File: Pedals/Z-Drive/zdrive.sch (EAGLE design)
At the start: 27 parts, among them IC1 MC1458P

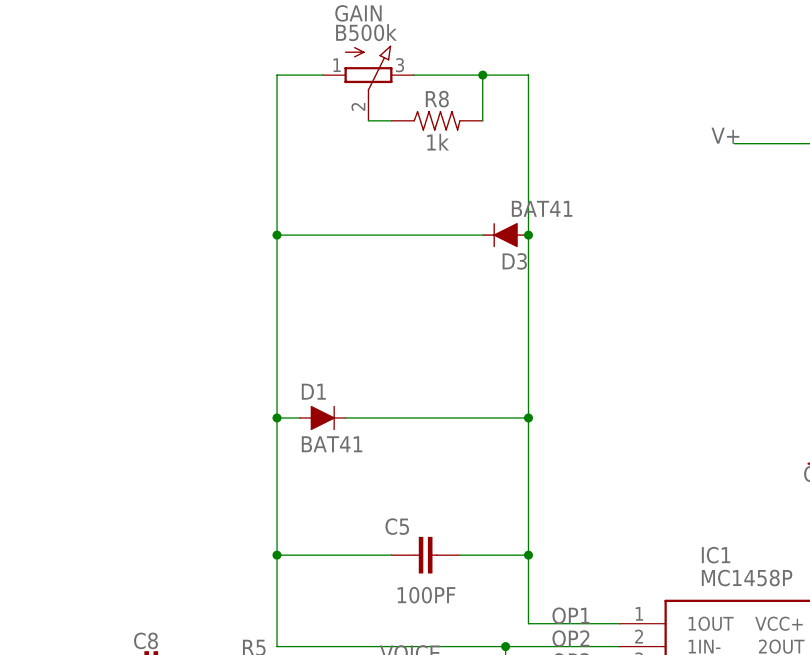
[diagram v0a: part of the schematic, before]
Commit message: Revert headmaster to correct revision
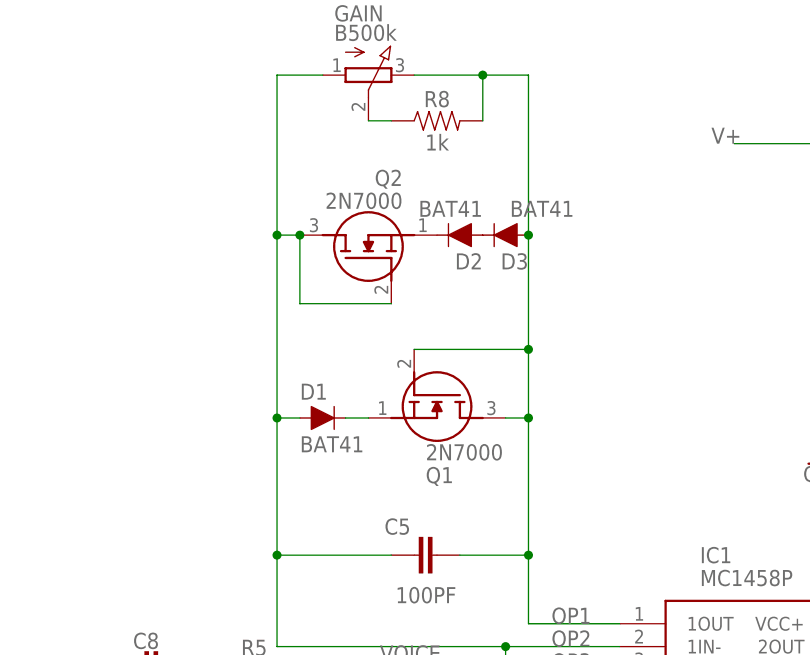
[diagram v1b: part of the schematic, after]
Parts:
- added D2: BAT41, SparkFun-DiscreteSemi:DIODE-KIT2
- added Q1, Q2: 2N7000, SamacSys_Parts:2N7000
- C4: value 0.1UF -> 0.1uF; device Custom-Parts:0.1UF -> SparkFun-Capacitors:0.1UF-KIT-EZ-50V-20%
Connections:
- new net N$10: D2.A, D3.C
- new net N$8: D1.C, Q1.S
- new net N$9: D2.C, Q2.S
- net OP1: now also Q1.D, Q1.G; no longer D1.C
- net OP2: now also Q2.D, Q2.G; no longer D3.C
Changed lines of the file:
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@@
 <part name="GND4" library="SparkFun-PowerSymbols" library_urn="urn:adsk.eagle:library:530" deviceset="GND" device=""/>
 <part name="R5" library="SparkFun-Resistors" library_urn="urn:adsk.eagle:library:532" deviceset="1KOHM" device="-HORIZ-1/4W-5%" package3d_urn="urn:adsk.eagle:package:39658/1" value="1k"/>
-<part name="C4" library="Custom-Parts" deviceset="0.1UF" device="" value="0.1UF"/>
+<part name="C4" library="SparkFun-Capacitors" library_urn="urn:adsk.eagle:library:510" deviceset="0.1UF" device="-KIT-EZ-50V-20%" package3d_urn="urn:adsk.eagle:package:37428/1" value="0.1uF"/>
 <part name="C5" library="Custom-Parts" deviceset="100PF" device=""/>
 <part name="GND5" library="SparkFun-PowerSymbols" library_urn="urn:adsk.eagle:library:530" deviceset="GND" device=""/>
@@
 <part name="C7" library="Custom-Parts" deviceset="47UF-POLAR" device="-RADIAL-2.5MM-25V-20%" package3d_urn="urn:adsk.eagle:package:37415/1" value="47uF"/>
 <part name="D1" library="SparkFun-DiscreteSemi" library_urn="urn:adsk.eagle:library:514" deviceset="DIODE" device="-KIT2" package3d_urn="urn:adsk.eagle:package:38455/1" value="BAT41"/>
+<part name="Q2" library="SamacSys_Parts" deviceset="2N7000" device=""/>
+<part name="D2" library="SparkFun-DiscreteSemi" library_urn="urn:adsk.eagle:library:514" deviceset="DIODE" device="-KIT2" package3d_urn="urn:adsk.eagle:package:38455/1" value="BAT41"/>
 <part name="D3" library="SparkFun-DiscreteSemi" library_urn="urn:adsk.eagle:library:514" deviceset="DIODE" device="-KIT2" package3d_urn="urn:adsk.eagle:package:38455/1" value="BAT41"/>
 <part name="R8" library="SparkFun-Resistors" library_urn="urn:adsk.eagle:library:532" deviceset="1KOHM" device="-HORIZ-1/4W-5%" package3d_urn="urn:adsk.eagle:package:39658/1" value="1k"/>
+<part name="Q1" library="SamacSys_Parts" deviceset="2N7000" device=""/>
 <part name="GAIN" library="Custom-Parts" deviceset="16MMPOT" device="" package3d_urn="urn:adsk.eagle:package:22726/1" value="B500k"/>
 <part name="VOICE" library="Custom-Parts" deviceset="16MMPOT" device="" package3d_urn="urn:adsk.eagle:package:22726/1" value="B10k"/>
@@
 <attribute name="VALUE" x="-15.24" y="104.648" size="1.778" layer="96" font="vector" align="top-left"/>
 </instance>
+<instance part="Q2" gate="G$1" x="-5.08" y="119.38" smashed="yes" rot="R90">
+<attribute name="NAME" x="-3.81" y="133.35" size="1.778" layer="95" rot="R180" align="center-left"/>
+<attribute name="VALUE" x="-3.81" y="130.81" size="1.778" layer="96" rot="R180" align="center-left"/>
+</instance>
+<instance part="D2" gate="G$1" x="2.54" y="127" smashed="yes" rot="R180">
+<attribute name="NAME" x="5.08" y="124.968" size="1.778" layer="95" font="vector" rot="R180"/>
+<attribute name="VALUE" x="5.08" y="129.032" size="1.778" layer="96" font="vector" rot="R180" align="top-left"/>
+</instance>
 <instance part="D3" gate="G$1" x="7.62" y="127" smashed="yes" rot="R180">
 <attribute name="NAME" x="10.16" y="124.968" size="1.778" layer="95" font="vector" rot="R180"/>
@@
 <attribute name="NAME" x="0" y="141.224" size="1.778" layer="95" font="vector" align="bottom-center"/>
 <attribute name="VALUE" x="0" y="138.176" size="1.778" layer="96" font="vector" align="top-center"/>
+</instance>
+<instance part="Q1" gate="G$1" x="-2.54" y="114.3" smashed="yes" rot="R270">
+<attribute name="NAME" x="-1.27" y="100.33" size="1.778" layer="95" align="center-left"/>
+<attribute name="VALUE" x="-1.27" y="102.87" size="1.778" layer="96" align="center-left"/>
 </instance>
 <instance part="GAIN" gate="G$1" x="-7.62" y="144.78" smashed="yes" rot="R270">
@@
 <pinref part="C5" gate="G$1" pin="2"/>
 <wire x1="10.16" y1="91.44" x2="10.16" y2="106.68" width="0.1524" layer="91"/>
+<wire x1="7.62" y1="106.68" x2="10.16" y2="106.68" width="0.1524" layer="91"/>
+<wire x1="10.16" y1="106.68" x2="10.16" y2="114.3" width="0.1524" layer="91"/>
+<junction x="10.16" y="106.68"/>
 <pinref part="D3" gate="G$1" pin="A"/>
-<wire x1="10.16" y1="106.68" x2="10.16" y2="127" width="0.1524" layer="91"/>
+<wire x1="10.16" y1="114.3" x2="10.16" y2="127" width="0.1524" layer="91"/>
 <wire x1="10.16" y1="127" x2="10.16" y2="144.78" width="0.1524" layer="91"/>
 <junction x="10.16" y="127"/>
@@
 <wire x1="20.32" y1="83.82" x2="10.16" y2="83.82" width="0.1524" layer="91"/>
 <label x="12.7" y="83.82" size="1.778" layer="95"/>
+<wire x1="-2.54" y1="114.3" x2="10.16" y2="114.3" width="0.1524" layer="91"/>
+<junction x="10.16" y="114.3"/>
+<pinref part="Q1" gate="G$1" pin="G"/>
+<pinref part="Q1" gate="G$1" pin="D"/>
 <pinref part="GAIN" gate="G$1" pin="E"/>
-<pinref part="D1" gate="G$1" pin="C"/>
-<wire x1="-10.16" y1="106.68" x2="10.16" y2="106.68" width="0.1524" layer="91"/>
-<junction x="10.16" y="106.68"/>
 </segment>
 <segment>
@@
 </segment>
 </net>
+<net name="N$8" class="0">
+<segment>
+<pinref part="D1" gate="G$1" pin="C"/>
+<wire x1="-10.16" y1="106.68" x2="-7.62" y2="106.68" width="0.1524" layer="91"/>
+<pinref part="Q1" gate="G$1" pin="S"/>
+</segment>
+</net>
+<net name="N$9" class="0">
+<segment>
+<pinref part="Q2" gate="G$1" pin="S"/>
+<pinref part="D2" gate="G$1" pin="C"/>
+</segment>
+</net>
+<net name="N$10" class="0">
+<segment>
+<pinref part="D2" gate="G$1" pin="A"/>
+<pinref part="D3" gate="G$1" pin="C"/>
+</segment>
+</net>
 <net name="OP2" class="0">
 <segment>
+<pinref part="Q2" gate="G$1" pin="G"/>
+<wire x1="-5.08" y1="119.38" x2="-15.24" y2="119.38" width="0.1524" layer="91"/>
+<pinref part="Q2" gate="G$1" pin="D"/>
+<wire x1="-15.24" y1="119.38" x2="-15.24" y2="127" width="0.1524" layer="91"/>
 <pinref part="C5" gate="G$1" pin="1"/>
 <wire x1="-17.78" y1="91.44" x2="-5.08" y2="91.44" width="0.1524" layer="91"/>
@@
 <junction x="-17.78" y="106.68"/>
 <wire x1="-17.78" y1="127" x2="-17.78" y2="144.78" width="0.1524" layer="91"/>
+<wire x1="-15.24" y1="127" x2="-17.78" y2="127" width="0.1524" layer="91"/>
+<junction x="-15.24" y="127"/>
+<junction x="-17.78" y="127"/>
 <wire x1="-17.78" y1="144.78" x2="-12.7" y2="144.78" width="0.1524" layer="91"/>
 <wire x1="-17.78" y1="91.44" x2="-17.78" y2="81.28" width="0.1524" layer="91"/>
@@
 <wire x1="7.62" y1="73.66" x2="7.62" y2="81.28" width="0.1524" layer="91"/>
 <junction x="7.62" y="81.28"/>
-<pinref part="D3" gate="G$1" pin="C"/>
-<wire x1="5.08" y1="127" x2="-17.78" y2="127" width="0.1524" layer="91"/>
-<junction x="-17.78" y="127"/>
-</segment>
-</net>
+</segment>
+</net>

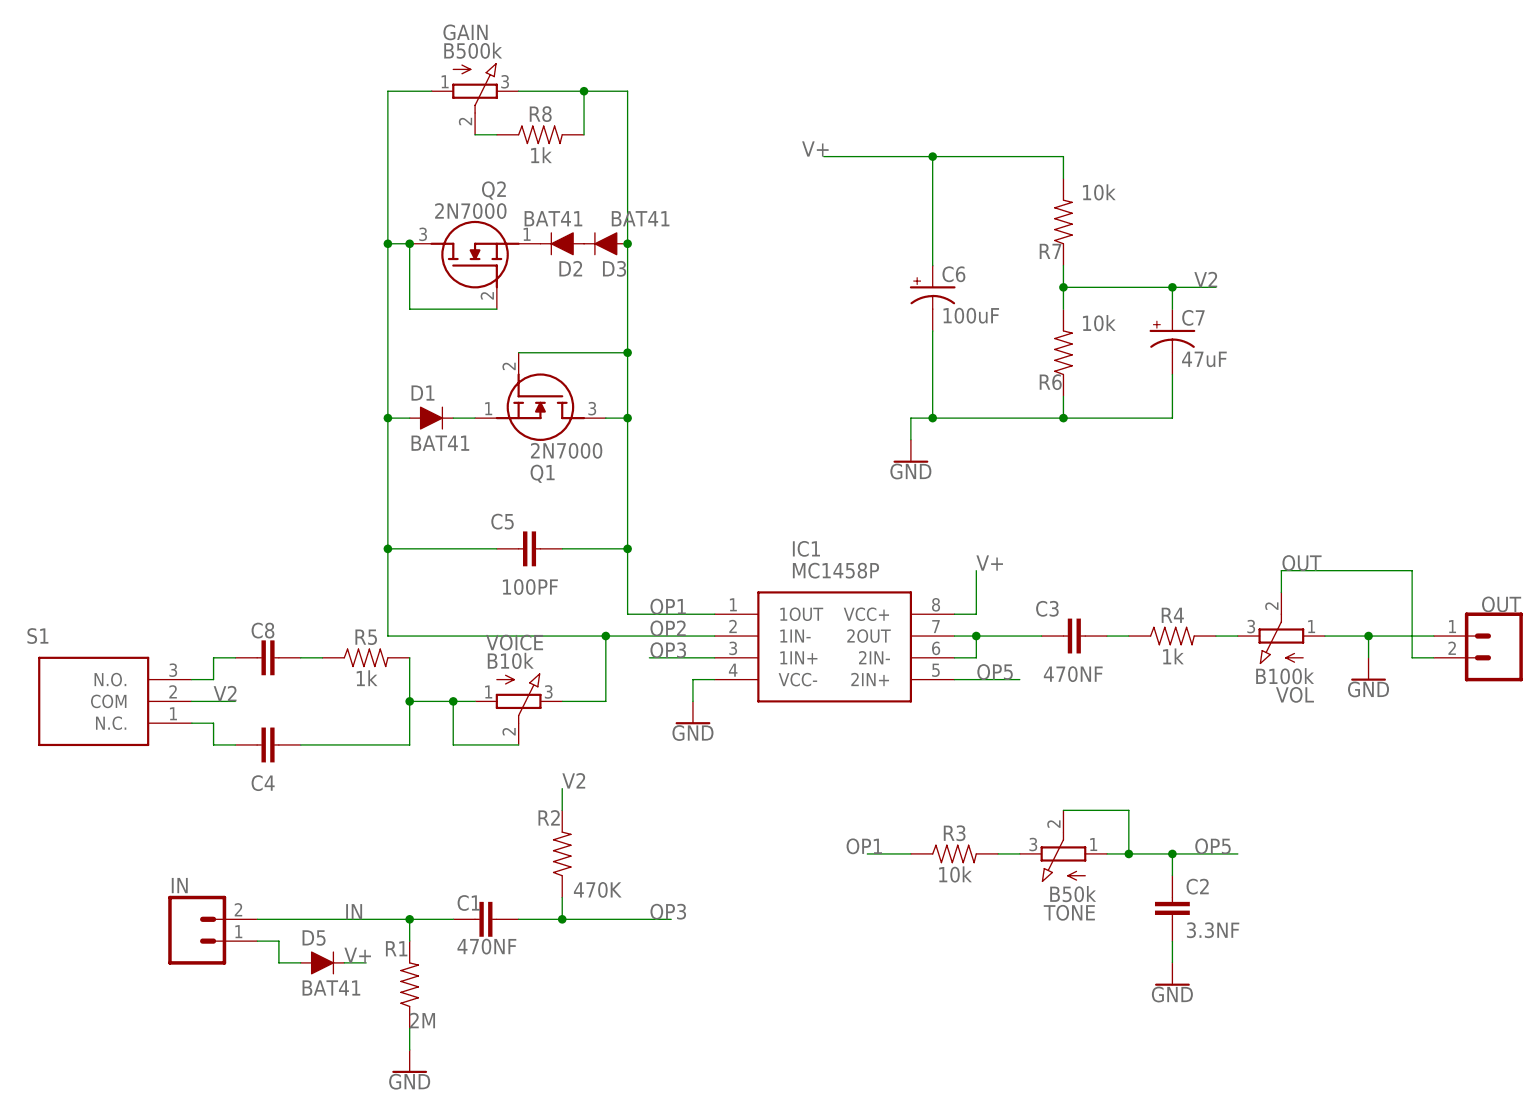
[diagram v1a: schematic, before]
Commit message: Update capacitors to be larger size
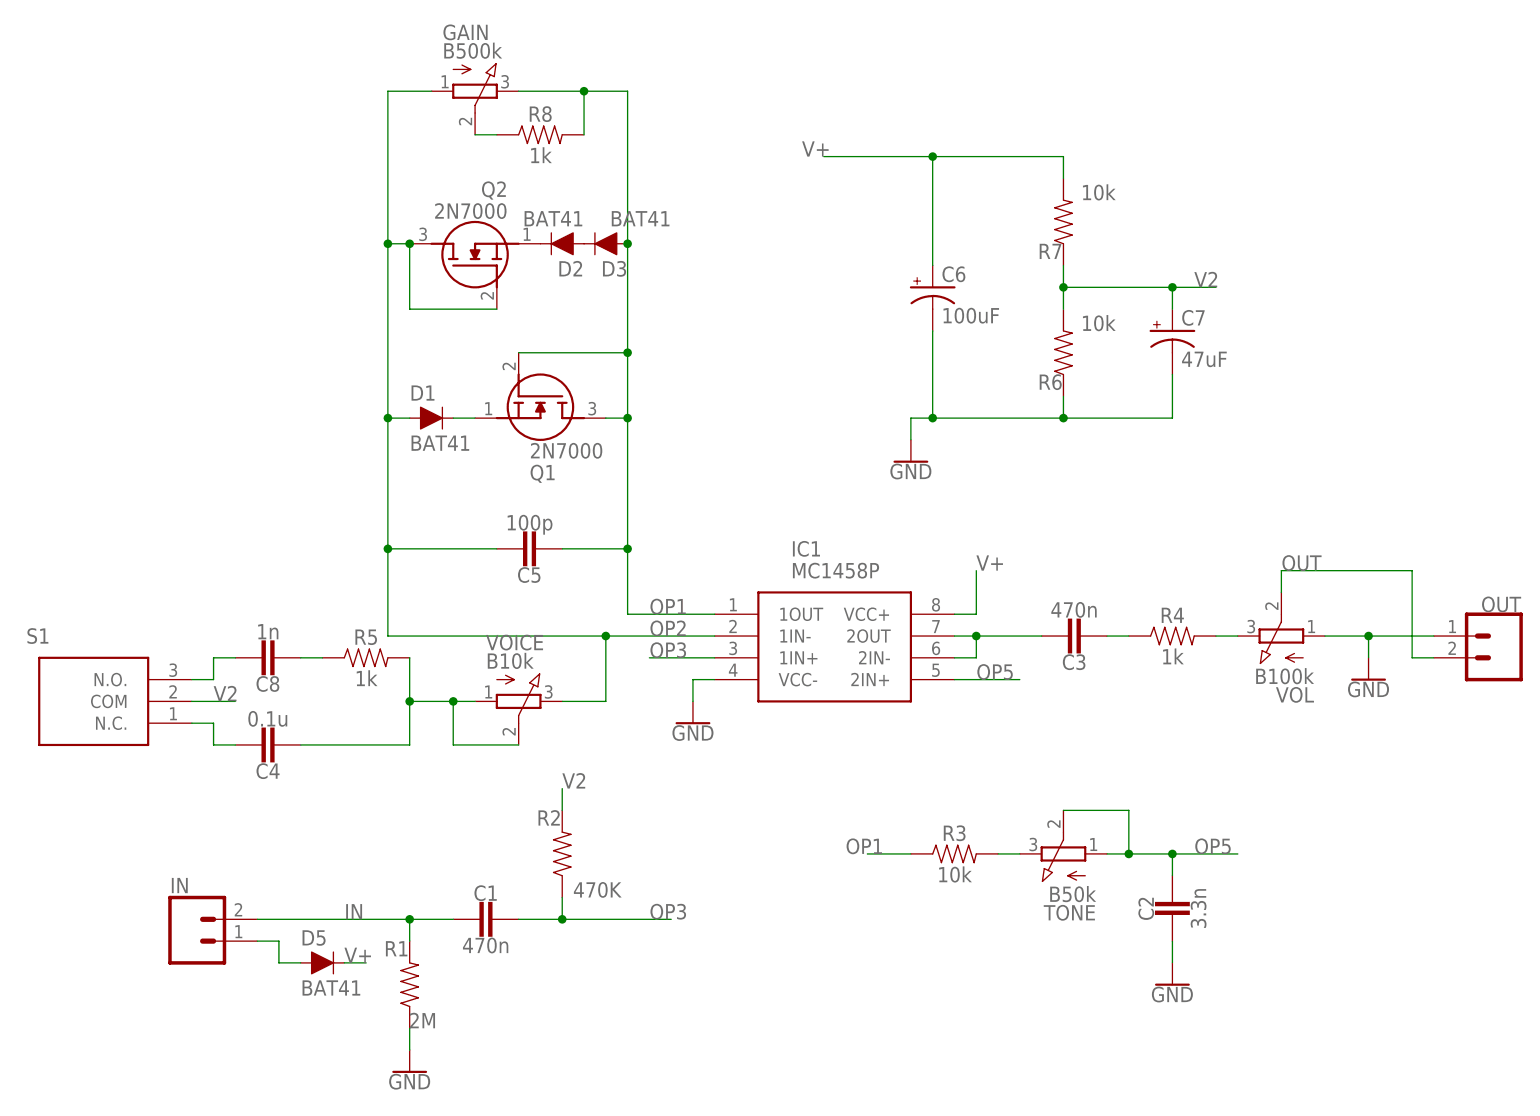
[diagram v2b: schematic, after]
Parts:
- C1, C3: value 470NF -> 470n; device Custom-Parts:470NF -> capacitors-film:CAP.5
- C2: value 3.3NF -> 3.3n; device Custom-Parts:3.3NF -> capacitors-film:CAP.5
- C4: value 0.1uF -> 0.1u; device SparkFun-Capacitors:0.1UF-KIT-EZ-50V-20% -> capacitors-film:CAP.5
- C5: value 100PF -> 100p; device Custom-Parts:100PF -> capacitors-film:CAP.5
- C8: value 1NF -> 1n; device Custom-Parts:1NF -> capacitors-film:CAP.5
